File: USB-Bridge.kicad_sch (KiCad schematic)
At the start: 8 parts, among them J3 USB_B_Micro, U3 CP2102N-Axx-xQFN28

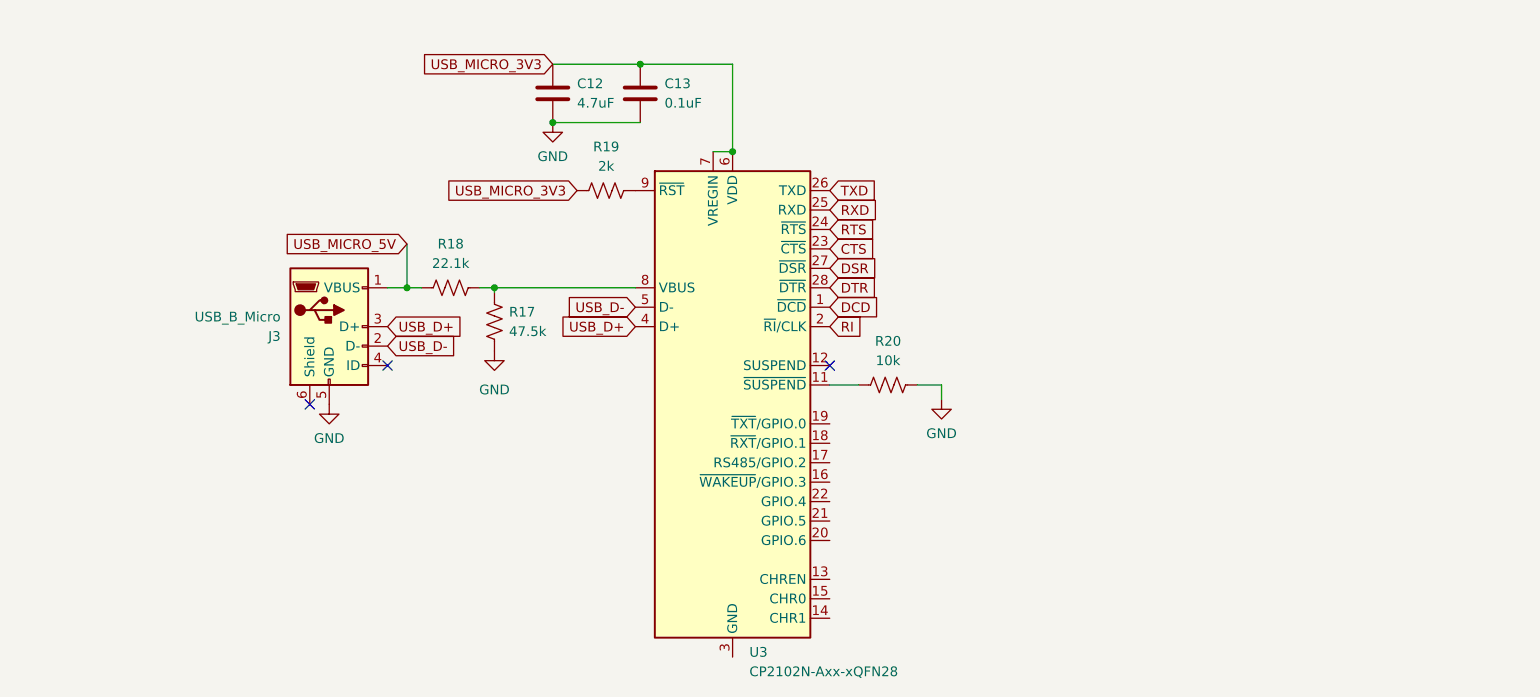
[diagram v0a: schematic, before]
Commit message: Finished Micro USB UART Bridge, started working on cell sch
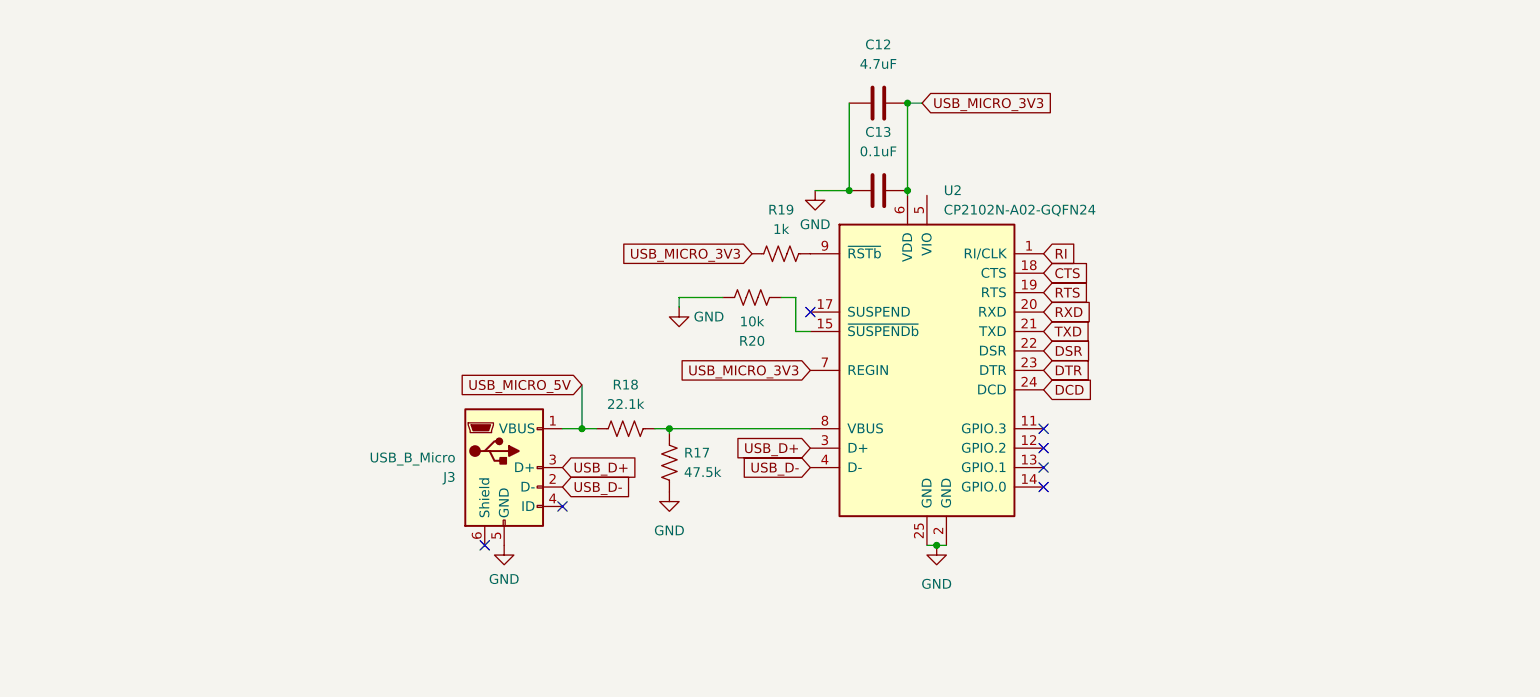
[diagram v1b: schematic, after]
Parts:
- removed U3: CP2102N-Axx-xQFN28, Package_DFN_QFN:QFN-28-1EP_5x5mm_P0.5mm_EP3.35x3.35mm, symbol Interface_USB:CP2102N-Axx-xQFN28
- added U2: CP2102N-A02-GQFN24, Package_DFN_QFN:QFN-24-1EP_4x4mm_P0.5mm_EP2.6x2.6mm, symbol utsvt-chips:CP2102N-A01-GQFN24
- R19: value 2k -> 1k
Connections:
- net CTS: now also U2.18 (CTS)
- net DCD: now also U2.24 (DCD)
- net DSR: now also U2.22 (DSR)
- net DTR: now also U2.23 (DTR)
- net GND: now also C12.1, C13.1, U2.2 (GND), U2.25 (GND); no longer C12.2, C13.2
- net RI: now also U2.1 (RI/CLK)
- net RTS: now also U2.19 (RTS)
- net RXD: now also U2.20 (RXD)
- net TXD: now also U2.21 (TXD)
- net USB_D+: now also U2.3 (D+)
- net USB_D-: now also U2.4 (D-)
- net USB_MICRO_3V3: now also C12.2, C13.2, U2.6 (VDD), U2.7 (REGIN); no longer C12.1, C13.1
- net at R17.1, R18.2: now also U2.8 (VBUS)
- net at R20.2: now also U2.15 (~{SUSPENDb})
- net at R19.1: now also U2.9 (~{RSTb})
- no-connect marks 3 -> 7
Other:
- moved on the sheet: C12, C13, J3, R17, R18, R19, R20

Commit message: usb uart fixes and ldo
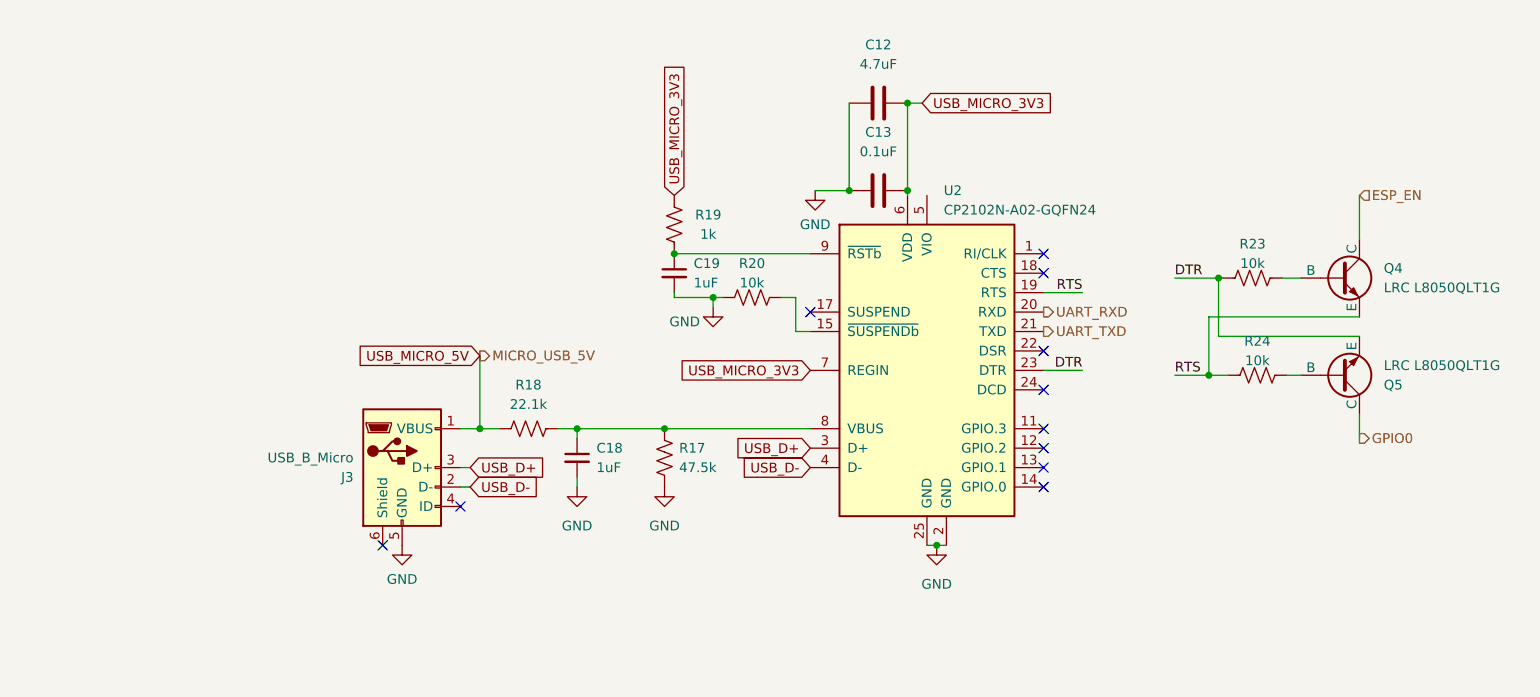
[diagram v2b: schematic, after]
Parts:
- added C18, C19: 1uF, symbol Device:C_Small
- added Q4, Q5: LRC L8050QLT1G, symbol Simulation_SPICE:NPN
- added R23, R24: 10k, symbol Device:R_US
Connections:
- net DTR: now also Q5.3 (E), R23.2
- net GND: now also R20.2, C18.2, C19.2; no longer R20.1
- net RTS: now also Q4.3 (E), R24.2
- net at R17.1, R18.2, U2.8 (VBUS): now also C18.1
- net at U2.15 (~{SUSPENDb}): now also R20.1; no longer R20.2
- net at R19.1, U2.9 (~{RSTb}): now also C19.1
- net CTS: no longer names the net of U2.18 (CTS)
- net DCD: no longer names the net of U2.24 (DCD)
- net DSR: no longer names the net of U2.22 (DSR)
- net RI: no longer names the net of U2.1 (RI/CLK)
- net RXD renamed UART_RXD
- net TXD renamed UART_TXD
- new net: Q4.2 (B), R23.1
- new net: Q5.2 (B), R24.1
- new net ESP_EN: Q4.1 (C)
- new net GPIO0: Q5.1 (C)
- no-connect marks 7 -> 11
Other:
- moved on the sheet: J3, R17, R18, R19, R20

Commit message: initial sch completed
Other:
- moved on the sheet: C12, C13, C18, C19, J3, R17, R18, R19, R20, U2
